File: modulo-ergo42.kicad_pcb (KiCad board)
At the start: 2 copper layers, 37 parts, among them J1 AudioJack4_Ground, J2 AudioJack4_Ground, J3 AudioJack4_Ground, SW1 SW_Push, SW10 SW_Push, SW11 SW_Push, SW12 SW_Push, SW13 SW_Push, SW14 SW_Push, SW15 SW_Push, SW16 SW_Push, SW17 SW_Push, SW18 SW_Push, SW19 SW_Push, SW2 SW_Push, SW20 SW_Push, SW21 SW_Push, SW22 SW_Push, SW23 SW_Push, SW24 SW_Push, SW25 SW_Push, SW26 SW_Push, SW27 SW_Push, SW28 SW_Push, SW29 SW_DIP_x02, SW3 SW_Push, SW4 SW_Push, SW5 SW_Push, SW6 SW_Push, SW7 SW_Push, SW8 SW_Push, SW9 SW_Push, U1 TCA9555PWR, U2 TCA9555PWR

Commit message: Layout socket
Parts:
- moved SW27 191.1 mm to (180.3, 83.8)
- moved SW26 178.9 mm to (180.3, 64.8)
- moved SW20 178.3 mm to (142.2, 102.9)
- moved SW28 171.8 mm to (180.3, 102.9)
- moved SW23 168.3 mm to (161.3, 83.8)
- moved SW19 168.0 mm to (142.2, 83.8)
- moved SW25 162.2 mm to (180.3, 45.7)
- moved SW24 159.8 mm to (161.3, 102.9)
- moved SW16 158.7 mm to (123.2, 102.9)
- moved SW2 156.7 mm to (66.0, 64.8)
- moved SW22 155.2 mm to (161.3, 64.8)
- moved SW4 155.1 mm to (66.0, 102.9)
- moved SW7 154.4 mm to (85.1, 83.8)
- moved SW15 149.8 mm to (123.2, 83.8)
- moved SW12 140.7 mm to (104.1, 102.9)
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
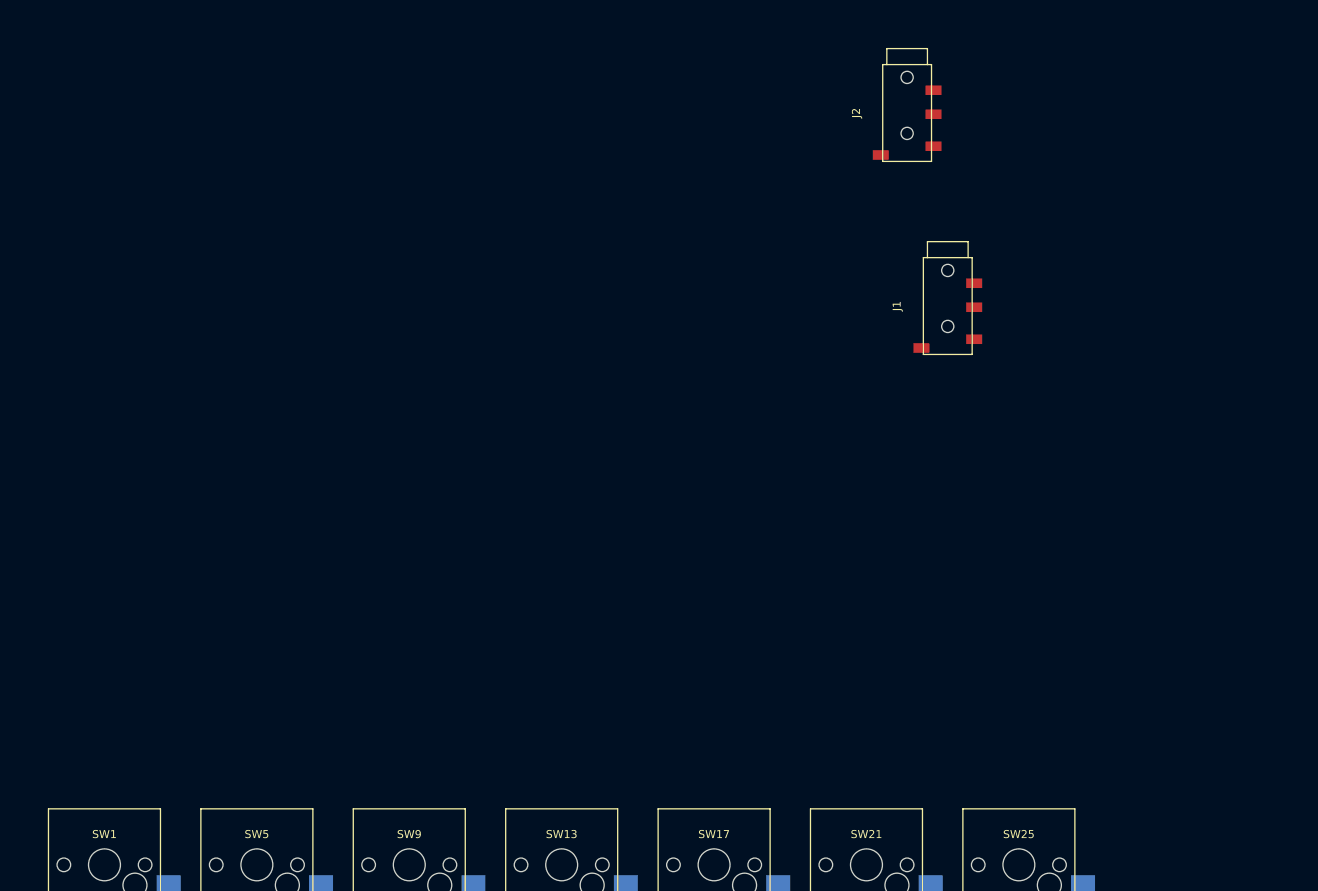
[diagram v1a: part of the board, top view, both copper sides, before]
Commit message: Add int socket
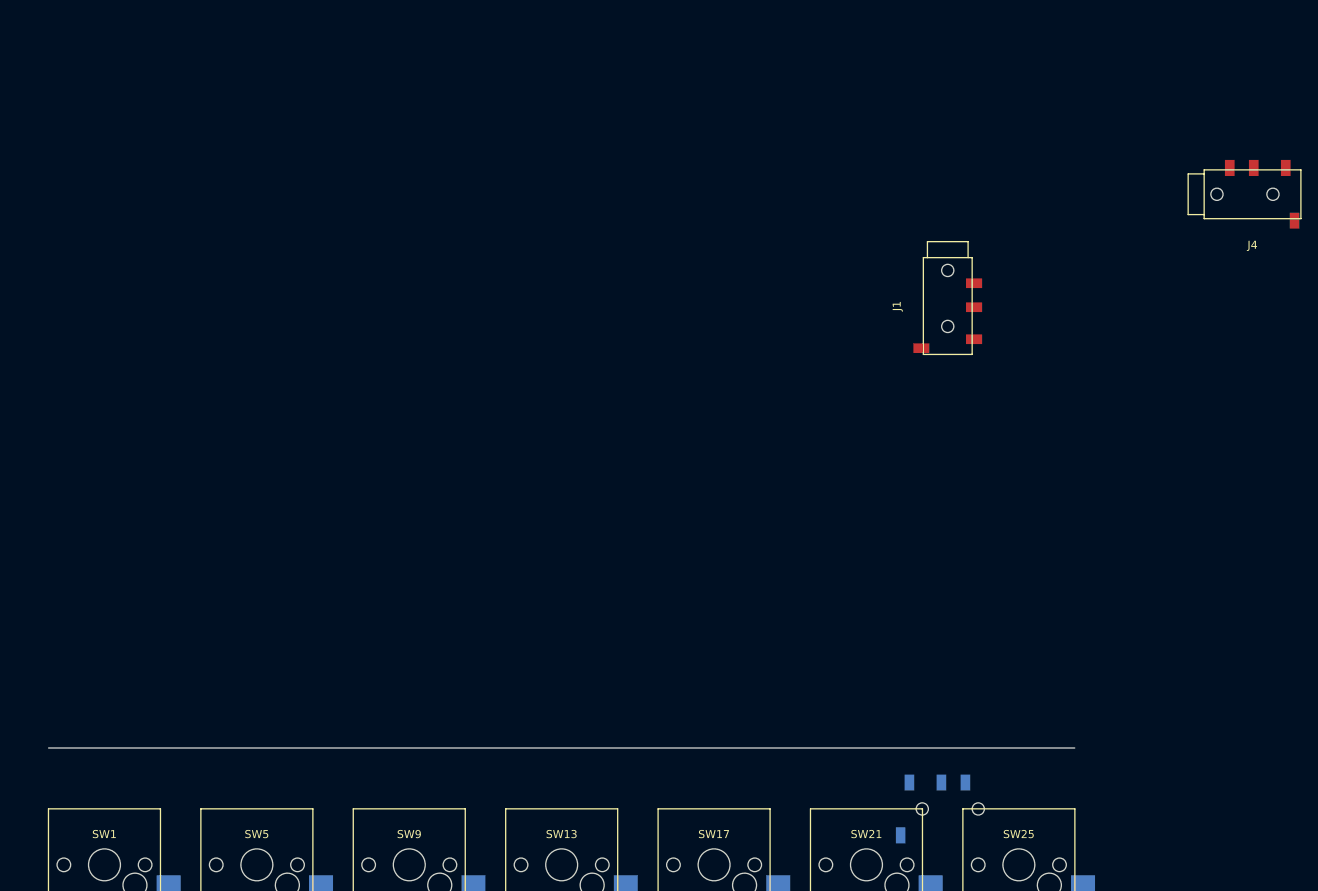
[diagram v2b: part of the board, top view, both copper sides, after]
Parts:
- added J4: AudioJack4_Ground, library:TRRS_SMD_PJ320, F.Cu at (209.6, -38.1)
- J2: moved to B.Cu
- moved J2 87.1 mm to (170.8, 38.7), turned to 180 degrees
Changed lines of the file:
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@@
   (general
     (thickness 1.6)
-    (drawings 0)
+    (drawings 1)
     (tracks 0)
     (zones 0)
-    (modules 37)
-    (nets 44)
+    (modules 38)
+    (nets 45)
   )
   (page A4)
@@
   (net 42 "Net-(U2-Pad19)")
   (net 43 "Net-(U2-Pad20)")
+  (net 44 "Net-(J4-PadR2)")
   (net_class Default "This is the default net class."
     (clearance 0.2)
@@
     (add_net INT)
     (add_net "Net-(J3-PadR2)")
+    (add_net "Net-(J4-PadR2)")
     (add_net "Net-(U2-Pad17)")
     (add_net "Net-(U2-Pad18)")
@@
     (pad "" np_thru_hole circle (at -4.45 0 270) (size 1.524 1.524) (drill 1.524) (layers *.Cu *.Mask))
   )
-  (module library:TRRS_SMD_PJ320 (layer F.Cu)
-    (at 166.37 -48.26 270)
-    (fp_text reference J2 (at 0 6.35 270) (layer F.SilkS)
-      (effects (font (size 1 1) (thickness 0.15)))
-    )
-    (fp_text value AudioJack4_Ground (at 0 -6.35 270) (layer F.Fab)
-      (effects (font (size 1 1) (thickness 0.15)))
-    )
-    (fp_line (start -6.05 -3.05) (end 6.05 -3.05) (layer F.SilkS) (width 0.15))
-    (fp_line (start 6.05 -3.05) (end 6.05 3.05) (layer F.SilkS) (width 0.15))
-    (fp_line (start 6.05 3.05) (end -6.05 3.05) (layer F.SilkS) (width 0.15))
-    (fp_line (start -6.05 3.05) (end -6.05 -3.05) (layer F.SilkS) (width 0.15))
-    (fp_line (start -6.05 -2.54) (end -8.05 -2.54) (layer F.SilkS) (width 0.15))
-    (fp_line (start -8.05 -2.54) (end -8.05 2.54) (layer F.SilkS) (width 0.15))
-    (fp_line (start -8.05 2.54) (end -6.05 2.54) (layer F.SilkS) (width 0.15))
-    (pad "" np_thru_hole circle (at -4.45 0 270) (size 1.524 1.524) (drill 1.524) (layers *.Cu *.Mask))
-    (pad "" np_thru_hole circle (at 2.55 0 270) (size 1.524 1.524) (drill 1.524) (layers *.Cu *.Mask))
-    (pad S smd rect (at 5.25 3.3 270) (size 1.2 2) (layers F.Cu F.Paste F.Mask)
-      (net 4 GND))
-    (pad T smd rect (at 4.15 -3.3 270) (size 1.2 2) (layers F.Cu F.Paste F.Mask)
+  (module library:TRRS_SMD_PJ320 (layer B.Cu)
+    (at 170.815 38.735 180)
+    (fp_text reference J2 (at 0 -6.35 180) (layer B.SilkS)
+      (effects (font (size 1 1) (thickness 0.15)) (justify mirror))
+    )
+    (fp_text value AudioJack4_Ground (at 0 6.35 180) (layer B.Fab)
+      (effects (font (size 1 1) (thickness 0.15)) (justify mirror))
+    )
+    (fp_line (start -6.05 3.05) (end 6.05 3.05) (layer B.SilkS) (width 0.15))
+    (fp_line (start 6.05 3.05) (end 6.05 -3.05) (layer B.SilkS) (width 0.15))
+    (fp_line (start 6.05 -3.05) (end -6.05 -3.05) (layer B.SilkS) (width 0.15))
+    (fp_line (start -6.05 -3.05) (end -6.05 3.05) (layer B.SilkS) (width 0.15))
+    (fp_line (start -6.05 2.54) (end -8.05 2.54) (layer B.SilkS) (width 0.15))
+    (fp_line (start -8.05 2.54) (end -8.05 -2.54) (layer B.SilkS) (width 0.15))
+    (fp_line (start -8.05 -2.54) (end -6.05 -2.54) (layer B.SilkS) (width 0.15))
+    (pad "" np_thru_hole circle (at -4.45 0 180) (size 1.524 1.524) (drill 1.524) (layers *.Cu *.Mask))
+    (pad "" np_thru_hole circle (at 2.55 0 180) (size 1.524 1.524) (drill 1.524) (layers *.Cu *.Mask))
+    (pad S smd rect (at 5.25 -3.3 180) (size 1.2 2) (layers B.Cu B.Paste B.Mask)
+      (net 4 GND))
+    (pad T smd rect (at 4.15 3.3 180) (size 1.2 2) (layers B.Cu B.Paste B.Mask)
       (net 3 3V3))
-    (pad R1 smd rect (at 0.15 -3.3 270) (size 1.2 2) (layers F.Cu F.Paste F.Mask)
+    (pad R1 smd rect (at 0.15 3.3 180) (size 1.2 2) (layers B.Cu B.Paste B.Mask)
       (net 5 SDA2))
-    (pad R2 smd rect (at -2.85 -3.3 270) (size 1.2 2) (layers F.Cu F.Paste F.Mask)
+    (pad R2 smd rect (at -2.85 3.3 180) (size 1.2 2) (layers B.Cu B.Paste B.Mask)
       (net 6 SCL2))
   )
@@
     )
   )
+  (module library:TRRS_SMD_PJ320 (layer F.Cu)
+    (at 209.55 -38.1)
+    (fp_text reference J4 (at 0 6.35) (layer F.SilkS)
+      (effects (font (size 1 1) (thickness 0.15)))
+    )
+    (fp_text value AudioJack4_Ground (at 0 -6.35) (layer F.Fab)
+      (effects (font (size 1 1) (thickness 0.15)))
+    )
+    (fp_line (start -6.05 -3.05) (end 6.05 -3.05) (layer F.SilkS) (width 0.15))
+    (fp_line (start 6.05 -3.05) (end 6.05 3.05) (layer F.SilkS) (width 0.15))
+    (fp_line (start 6.05 3.05) (end -6.05 3.05) (layer F.SilkS) (width 0.15))
+    (fp_line (start -6.05 3.05) (end -6.05 -3.05) (layer F.SilkS) (width 0.15))
+    (fp_line (start -6.05 -2.54) (end -8.05 -2.54) (layer F.SilkS) (width 0.15))
+    (fp_line (start -8.05 -2.54) (end -8.05 2.54) (layer F.SilkS) (width 0.15))
+    (fp_line (start -8.05 2.54) (end -6.05 2.54) (layer F.SilkS) (width 0.15))
+    (pad "" np_thru_hole circle (at -4.45 0) (size 1.524 1.524) (drill 1.524) (layers *.Cu *.Mask))
+    (pad "" np_thru_hole circle (at 2.55 0) (size 1.524 1.524) (drill 1.524) (layers *.Cu *.Mask))
+    (pad S smd rect (at 5.25 3.3) (size 1.2 2) (layers F.Cu F.Paste F.Mask)
+      (net 4 GND))
+    (pad T smd rect (at 4.15 -3.3) (size 1.2 2) (layers F.Cu F.Paste F.Mask)
+      (net 3 3V3))
+    (pad R1 smd rect (at 0.15 -3.3) (size 1.2 2) (layers F.Cu F.Paste F.Mask)
+      (net 7 INT))
+    (pad R2 smd rect (at -2.85 -3.3) (size 1.2 2) (layers F.Cu F.Paste F.Mask)
+      (net 44 "Net-(J4-PadR2)"))
+  )
+  (gr_line (start 59.055 31.115) (end 187.325 31.115) (layer Edge.Cuts) (width 0.15))
 )

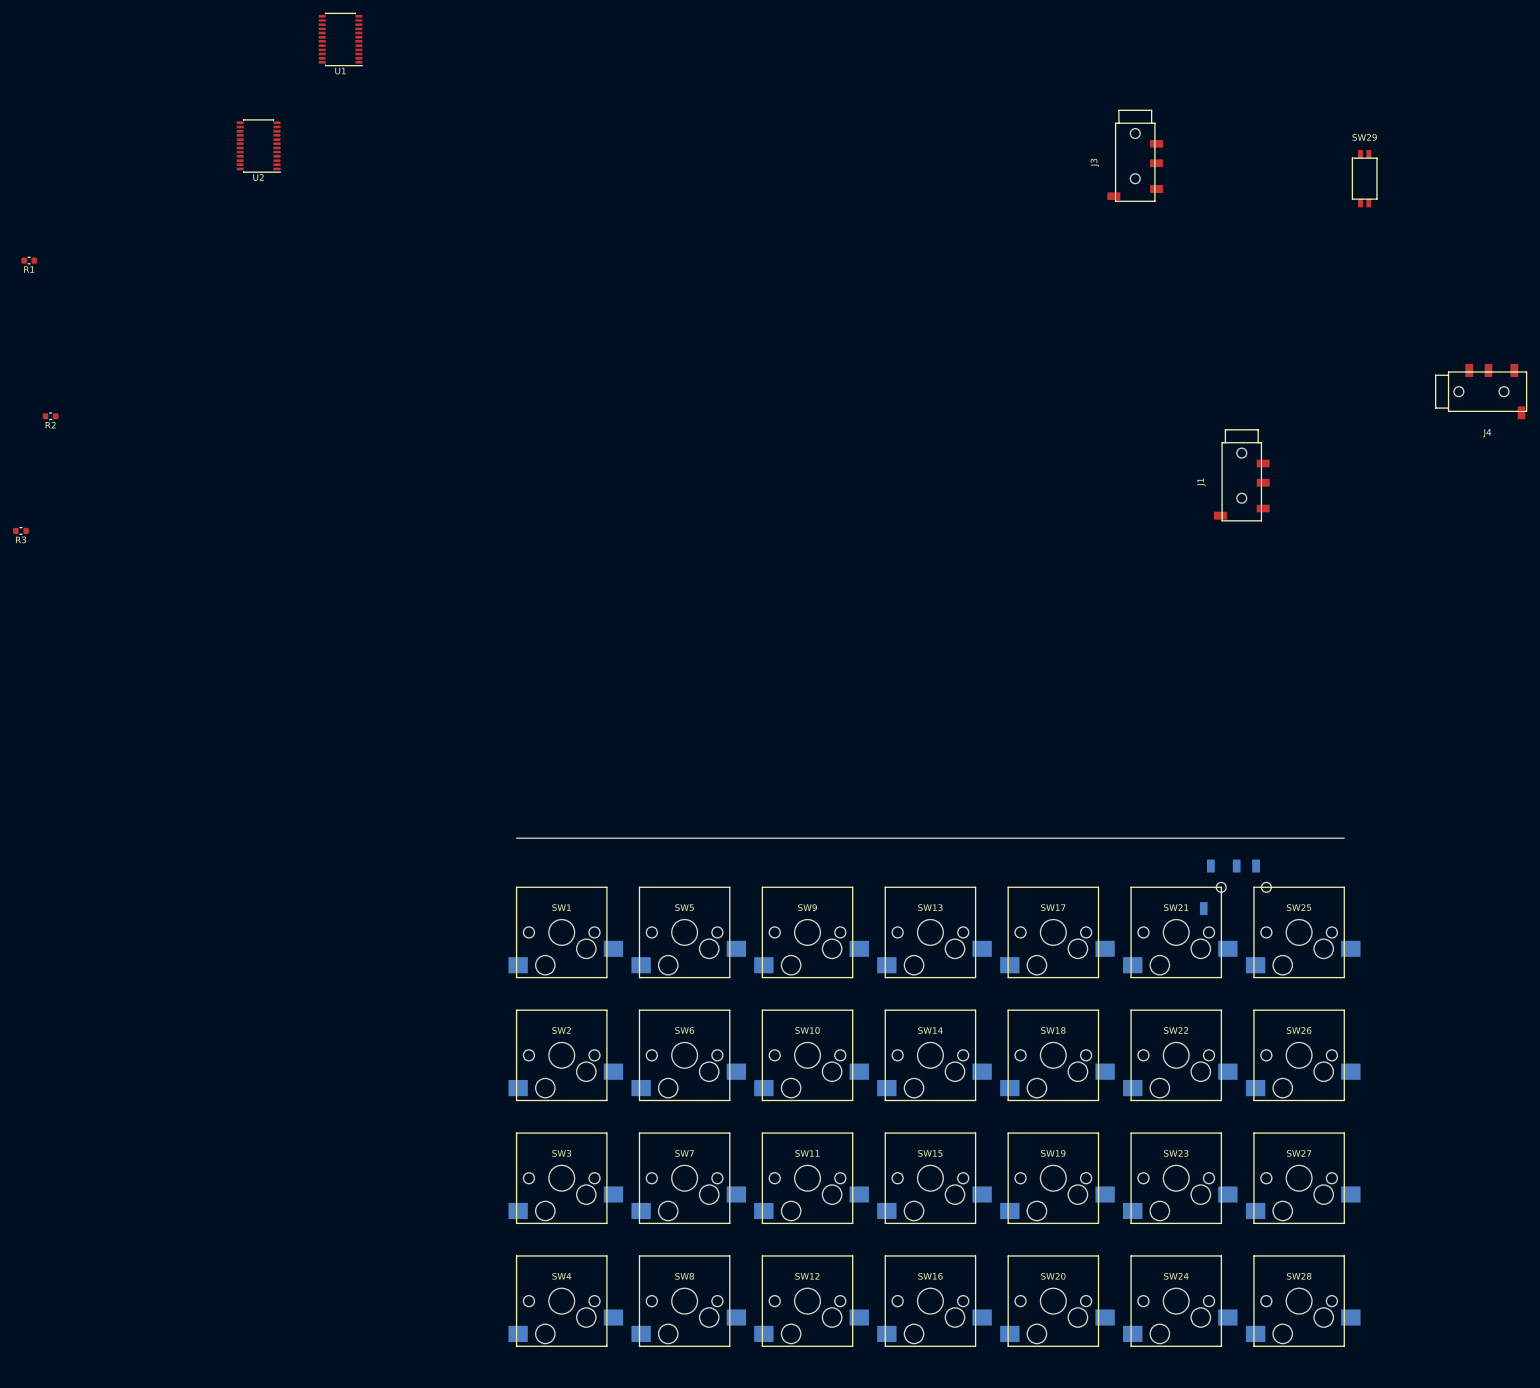
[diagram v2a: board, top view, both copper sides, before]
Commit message: Layout socket, TRRS jack and edge
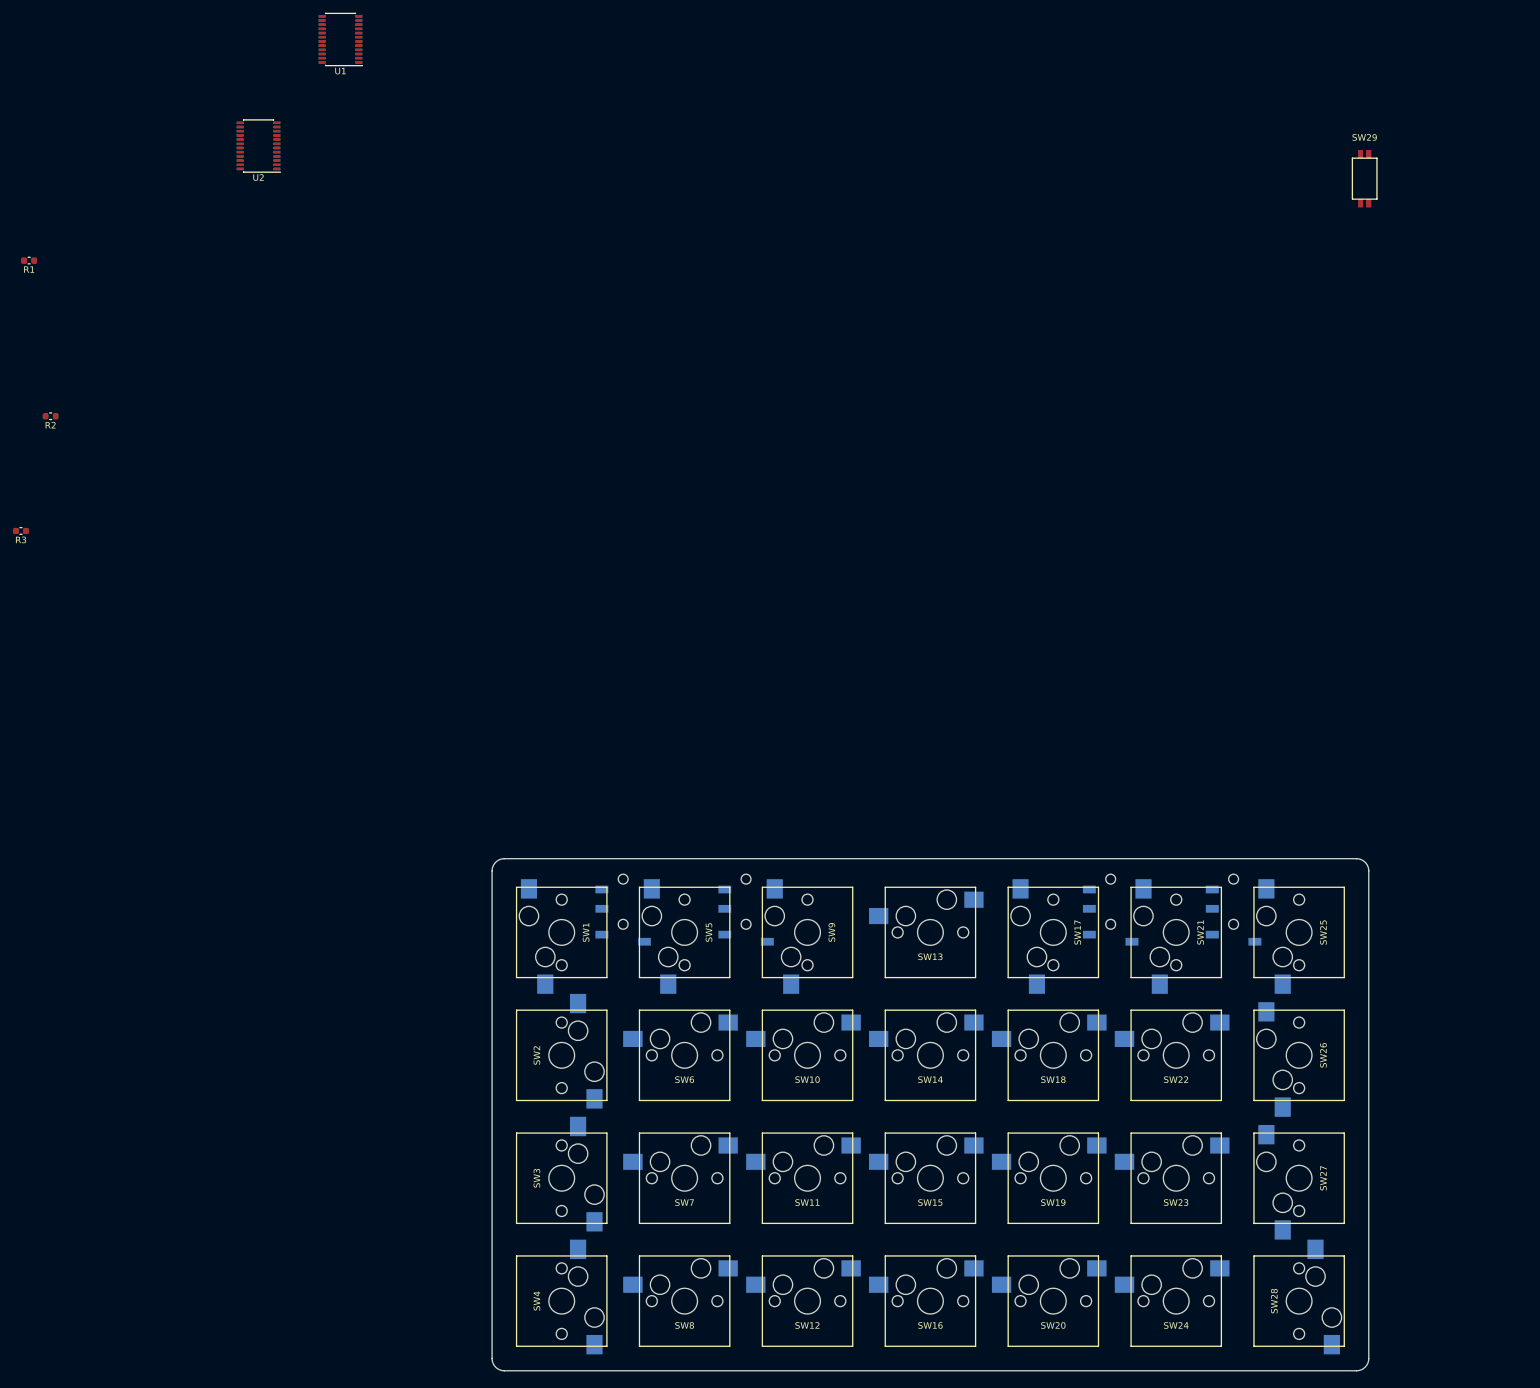
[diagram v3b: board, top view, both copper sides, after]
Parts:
- J1, J3, J4: moved to B.Cu
- moved J3 130.4 mm to (94.6, 41.9)
- moved J1 116.4 mm to (75.6, 41.9)
- moved J4 99.1 mm to (151.1, 41.9), turned to 270 degrees
- moved J2 3.24 mm to (170.2, 41.9), turned to 270 degrees
- turned SW1 to 90 degrees
- turned SW10 to 0 degrees
- turned SW11 to 0 degrees
- turned SW12 to 0 degrees
- turned SW13 to 0 degrees
- turned SW14 to 0 degrees
- turned SW15 to 0 degrees
- turned SW16 to 0 degrees
- turned SW17 to 90 degrees
- turned SW18 to 0 degrees
- turned SW19 to 0 degrees
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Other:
- board outline added: 135.9 x 79.4 mm

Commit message: [WIP] temp layout
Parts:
- SW29, U1, U2: moved to B.Cu
- moved U2 210.1 mm to (168.3, 71.8), turned to 0 degrees
- moved R3 192.3 mm to (151.8, 74.3)
- moved R1 185.9 mm to (113.7, 74.3)
- moved R2 181.9 mm to (132.7, 74.3)
- moved U1 175.5 mm to (94.6, 71.1), turned to 0 degrees
- moved SW29 127.9 mm to (129.5, 41.3), turned to 270 degrees
- turned SW13 to 90 degrees
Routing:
- added copper zone on B.Cu, net GND

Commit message: Re-place parts for drill
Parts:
- R1, R2, R3: moved to B.Cu
- moved R3 24.8 mm to (127.0, 74.3), turned to 270 degrees
- moved U1 9.55 mm to (85.1, 71.8)
- moved R2 9.53 mm to (123.2, 74.3), turned to 270 degrees
- moved U2 6.99 mm to (161.3, 71.8)
- moved R1 5.71 mm to (119.4, 74.3), turned to 270 degrees
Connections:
- U1 pad 10: R3C2 -> R2C2
- U1 pad 11: R4C2 -> R1C2
- U1 pad 4: R1C1 -> R4C1
- U1 pad 5: R2C1 -> R3C1
- U1 pad 6: R3C1 -> R2C1
- U1 pad 7: R4C1 -> R1C1
- U1 pad 8: R1C2 -> R4C2
- U1 pad 9: R2C2 -> R3C2
- U2 pad 10: R3C6 -> R2C6
- U2 pad 11: R4C6 -> R1C6
- U2 pad 4: R1C5 -> R4C5
- U2 pad 5: R2C5 -> R3C5
- U2 pad 6: R3C5 -> R2C5
- U2 pad 7: R4C5 -> R1C5
- U2 pad 8: R1C6 -> R4C6
- U2 pad 9: R2C6 -> R3C6
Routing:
- net 3V3: track 0.00 -> 21.3 mm, vias 0 -> 2
- added copper zone on F.Cu, net GND
